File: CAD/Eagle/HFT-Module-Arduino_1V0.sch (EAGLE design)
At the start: 399 parts, among them Q0521 ABS07-32.768KHZ, Q0811 ABM03B-32.000MHZ, Q0911 ABM3B-16MHZ-10-R50-1-U, T1201 MMBT2222, T1202 MMBT2222, T1203 MMBT2222, U0111 STM32L4Z_144PIN_SMPS, U0431 PAM2305AAB120, U0601 LM4120IM5-3.0, U0611 MAX5217, U0631 CFPT-141-20MHZ, U0641 OPA354, U0701 Si5338, U0801 SX1276, U0901 AX5243, U0911 PE4259, U0921 PE4259, U0991 PE4259, U1101 MCP3911A0-E-SS, U1111 MAX5136AGTG+, U1121 OPA354, U1131 OPA354, U1141 OPA354, U1201 NHD-C0220BIZ_2X20CHARS, U1301 MPU-9250, U1311 MS5607-02BA03, U1321 SHT31-DIS, U1401 SOLARPANEL_3V3_5MA1_25MM_X_20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, U1402 SPV1040T, U1501 TS5A23166, U1601 SC189ZSKTRT, U1701 TS5A23166, U1801 TS5A23166, U1901 TS5A23166, X1261 TTE_EN11-HSM, X2001 MOLEX 105017-0001, X2101 SMA_SMT_AMPHENOL-901-143, SAM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, X2111 SMA_SMT_AMPHENOL-901-143, SAM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, X2201 CUI SJ1-3535NS, X2211 CUI SJ1-3535NS, X2311 2X20/90_1MM27_HARWIN_M50-3202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, X2312 2X20/90_1MM27_HARWIN_M50-3202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, X2321 2X20/90_1MM27_HARWIN_M50-3202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, X2322 2X20/90_1MM27_HARWIN_M50-3202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, X2331 2X20/90_1MM27_HARWIN_M50-3202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, X2332 2X20/90_1MM27_HARWIN_M50-3202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

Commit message: HW_1V0 - Initial setup of PCB
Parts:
- removed C0313, C0421, C0422, C0432, C0441, C0601, C0611, C0612, C0631, C0641, C0701, C0702, C0703, C0705, C1001, C1002, C1003, C1101, C1102, C1103, C1111, C1112, C1231, C1301, C1303, C1311, C1321, C1402, C1403, C1501, C1605, C1701, C1703, C1801, C1803, C1901, C1902, C1903, C1908, C1909: 100nF, rcl:C-EUC0603
- removed C0401, C0402, C0403, C0404, C0405, C0406, C0407, C0408, C0409, C0802, C0803, C0804, C0805, C0806, C0807: 100n, rcl:C-EUC0603
- removed C0410, C0423: 4.7uF, rcl:C-EUC0805
- removed C0412, C0715, C0716, C1302: 10nF, rcl:C-EUC0603
- removed C0413, C0442, C0622, C1211, C1221: 1uF, rcl:C-EUC0805
- removed C0431, C0444, C1401, C1404: 10uF, rcl:C-EUC0805
- removed C0451, C1601, C1607: 1F_EEC-S5R5H105N, df4iah_rcl:CPOL-EUW14MM_D8MM_P13MM5
- removed C0511, C0861: 1.5pF, rcl:C-EUC0603
- removed C0531: TZY2Z100AC01R00, df4iah_c-trimm:C-TRIMM3MM2_2MM5
- removed C0632: 100pF, rcl:C-EUC0603
- removed C0704: 220nF, rcl:C-EUC0603
- removed C0801: 1u, rcl:C-EUC0603
- removed C0811: 4.7p, df4iah_c-trimm:C-TRIMM3MM2_2MM5
- removed C0812: 4.7p, rcl:C-EUC0603
- removed C0841, C0850, C0858, C0872, C_AX_C1, C_AX_C2, C_AX_M2: 0pF, rcl:C-EUC0603
- removed C0843: 3.3pF, rcl:C-EUC0603
- removed C0844, C0846, C0851, C0852, C0873, C0875, C1113: 47pF, rcl:C-EUC0603
- removed C0853, C0863, C0871, C_AX_A2, C_AX_A3, C_AX_B2, C_AX_F2, C_AX_M1: 4.7pF, rcl:C-EUC0603
- removed C0854: 15nH, rcl:C-EUC0603
- removed C0856, C0859: 6.8pF, rcl:C-EUC0603
- removed C0857: 2.7pF, rcl:C-EUC0603
- removed C0862: 33pF, rcl:C-EUC0603
- removed C0864: 1.2pF, rcl:C-EUC0603
- removed C0865: 1.8pF, rcl:C-EUC0603
- removed C0911, C0921, C0999, C1261, C1262, C1271: 1nF, rcl:C-EUC0603
- removed C0991: 100pF HiQ, rcl:C-EUC0603
- removed C0992, C0993: 330pF HiQ, rcl:C-EUC0603
- removed C0994, C0996: 0nF HiQ, rcl:C-EUC0603
- removed C1104, C1105, C1131, C1141: 220nF, df4iah_rcl:C-EUC0603
- removed C1128, C1129: 100nF, df4iah_rcl:C-EUC0603
- removed C1132, C1142: 100uF, df4iah_rcl:C-EUC0805
- removed C1405: 0nF, rcl:C-EUC0603
- removed C1406, C1602, C1606: 47uF, rcl:C-EUC0805
- removed C2003: 1nF, df4iah_rcl:C-EUC0603
- removed C_AX_T1, C_AX_T2: 4.3pF, rcl:C-EUC0603
- removed D0451: CMAD6001, df4iah_diode:D_SOD923
- removed D1403, D1501: CRS08, df4iah_diode:CRS08
- removed H2401, H2402, H2403, H2404: MOUNT-PAD-ROUND2.8, holes:MOUNT-PAD-ROUND2.8
- removed L0411, L1102, L1112: 10uH, rcl:L-EUL2012C
- removed L0433: 2.2uH 14mR, df4iah_rcl:L-EU6.0X6.0MM
- removed L0842, L0862: 10nH, rcl:R-US_R0603
- removed L0851: 68nH, rcl:R-US_R0603
- removed L0856, L0858, L0995: 0R, rcl:R-US_R0603
- removed L0857: 12nH, rcl:R-US_R0603
- removed L0861: 33nH, rcl:R-US_R0603
- removed L0864: 6.2nH, rcl:R-US_R0603
- removed L0871: 18nH, rcl:R-US_R0603
- removed L1403: 33uH, df4iah_rcl:L-EU13.5X12.5MM
- removed L1604: 1.0uH 33mR, rcl:L-EUL5650M
- removed L_AX_1, L_AX_B1, L_AX_B2, L_AX_F1: 22nH, rcl:R-US_R0603
- removed L_AX_C1, L_AX_C2: 100nH, rcl:R-US_R0603
- removed L_AX_T1, L_AX_T2: 43nH, rcl:R-US_R0603
- removed PF2011: 1.1A/2.2A, rcl:R-EU_M1206
- removed Q0521: ABS07-32.768KHZ, df4iah_crystal:ABS07-32.768KHZ
- removed Q0811: ABM03B-32.000MHZ, df4iah_crystal:ABM03B-32.000MHZ
- removed Q0911: ABM3B-16MHZ-10-R50-1-U, df4iah_crystal:ABM03B-16.000MHZ
- removed R0201, R0202, R0211, R0212, R0221, R0222, R0231, R0232, R0441, R0612, R0613, R0811, R0845, R0874, R1404, R1405, R1406, R1409: 0R, rcl:R-EU_R0603
- removed R0241, R0242, R0243, R0251, R0252, R0253, R0254, R0261, R0262, R0263, R0269, R0271, R0272, R0273, R0274, R0275, R0276, R0277, R0281, R0282, R0283, R0284, R0285, R0286, R0287, R0288, R0289, R0290, R0291, R0292, R0293, R0294, R0295, R0296, R0642, R0713, R0714, R0723, R0724, R0731, R0732, R0735, R0736, R0743, R0744, R0802, R0803, R0831, R1021, R1041, R1051, R1061, R1106, R1107, R1108, R1109, R1114, R2310, R2311, R2312, R2313, R2314, R2315, R2316, R2317, R2318, R2320, R2321, R2322, R2323, R2324, R2325, R2326, R2327, R2328, R2330, R2331, R2332, R2333, R2334, R2335, R2336, R2337, R2338: 47R, rcl:R-EU_R0603
- removed R0311: 3.3kR, rcl:R-EU_R0603
- removed R0321, R0631, R1131, R1141, R1261, R1262, R1271: 10kR, rcl:R-EU_R0603
- removed R0611: open, rcl:R-EU_R0603
- removed R0621, R1031, R1032, R1407, R1412: 100kR, rcl:R-EU_R0603
- removed R0638, R0639: 50R, rcl:R-EU_R0603
- removed R0711, R0712: none, rcl:R-EU_R0603
- removed R0751, R0801, R0821: 100R, rcl:R-EU_R0603
- removed R0804, R0805, R0806, R0807: NC, rcl:R-EU_R0603
- removed R1104, R1105: 22kR, rcl:R-EU_R0603
- removed R1110, R1132, R1135, R1142, R1145, R1241, R1502, R1702, R1802, R1902: 33kR, rcl:R-EU_R0603
- removed R1201, R1205, R1208: 1.8kR, rcl:R-EU_R0603
- removed R1202: 5.2kR, rcl:R-EU_R0603
- removed R1203: 68R, rcl:R-EU_R0805
- removed R1204, R1207: 2.2kR, rcl:R-EU_R0603
- removed R1206, R1209: 10R, rcl:R-EU_R0805
- removed R1301: 68R, rcl:R-EU_R0603
- removed R1331, R1332: 3.9kR, rcl:R-EU_R0603
- removed R1408: 310kR, rcl:R-EU_R0603
- removed R1411: 1kR, rcl:R-EU_R0603
- removed R2002: 330kR, rcl:R-EU_R0603
- removed S0312: KSR223G, df4iah_switch:KSR223G_SMD_1POL
- removed SJ0121, SJ0401, SJ0421, SJ0422, SJ0423, SJ0424: (no value), df4iah_jumper:SJ
- removed T1201, T1202, T1203: MMBT2222, transistor:BC846
- removed TP_+1V2, TP_+1V2_MCU, TP_+3V3, TP_+3V3_20MHZ, TP_+3V3_HICUR, TP_+5V0, TP_+5V0_SOL, TP_+5V0_USB_SW, TP_VBAT, TP_VSOL: PTR1B1,27, testpad:PTR1B1,27
- removed TP_AX_ADC1, TP_AX_ADC2, TP_AX_IRQ, TP_AX_TCXO_EN, TP_SX_DIO0, TP_SX_DIO1, TP_SX_DIO2, TP_SX_DIO3, TP_SX_DIO4, TP_SX_DIO5, TP_SX_RXTX: PTR1TP06R, testpad:PTR1TP06R
- removed U0111: STM32L4Z_144PIN_SMPS, df4iah_stm32l4:STM32L4Z_144PIN_SMPS
- removed U0431: PAM2305AAB120, df4iah_powersupply:PAM2305
- removed U0601: LM4120IM5-3.0, df4iah_powersupply:LM4120IM5-3.0
- removed U0611: MAX5217, df4iah_dac:MAX5217
- removed U0631: CFPT-141-20MHZ, df4iah_osc:CFPT-141-20MHZ
- removed U0641, U1121, U1131, U1141: OPA354, df4iah_opamp:OPA354
- removed U0701: Si5338, df4iah_osc:SI5338
- removed U0801: SX1276, df4iah_rf:SX1276
- removed U0901: AX5243, df4iah_rf:AX5243
- removed U0911, U0921, U0991: PE4259, df4iah_rf:PE4259
- removed U1101: MCP3911A0-E-SS, df4iah_adc:MCP3911
- removed U1111: MAX5136AGTG+, df4iah_dac:MAX5136
- removed U1201: NHD-C0220BIZ_2X20CHARS, df4iah_lcd:NHD-C0220BIZ_2X20CHARS
- removed U1301: MPU-9250, df4iah_sensors:MPU-9250
- removed U1311: MS5607-02BA03, df4iah_sensors:MS5607-02BA03
- removed U1321: SHT31-DIS, df4iah_sensors:SHT31-DIS
- removed U1401: SOLARPANEL_3V3_5MA1_25MM_X_20MM, df4iah_supply:SOLARPANEL_3V3_5MA1_25MM_X_20MM
- removed U1402: SPV1040T, df4iah_powersupply:SPV1040
- removed U1501, U1701, U1801, U1901: TS5A23166, df4iah_sc-switches:TS5A23166
- removed U1601: SC189ZSKTRT, df4iah_powersupply:PAM2305
- removed X0301: (no value), df4iah_connector:HEADER-2X3
- removed X0322: (no value), df4iah_connector:HEADER-1X2
- removed X1261: TTE_EN11-HSM, df4iah_switch:TTE_EN11-HSM
- removed X2001: MOLEX 105017-0001, df4iah_connector:USB_MICRO-B_MOLEX
- removed X2101, X2111: SMA_SMT_AMPHENOL-901-143, SAMTEC SMA-J-P-H-RA-TH1, df4iah_connector:SMA_SMT_AMPHENOL-901-143
- removed X2201, X2211: CUI SJ1-3535NS, df4iah_connector:SJ1-353XNS_3MM5-STEREO-AUDIO-JACKS
- removed X2311, X2312, X2321, X2322, X2331, X2332: 2X20/90_1MM27_HARWIN_M50-3202045, df4iah_connector:2X20/90_1MM27_HARWIN_M50-3202045
- added H411, H412: MOUNT-PAD-ROUND2.8, holes:MOUNT-PAD-ROUND2.8
- added R111, R112, R113, R114, R115, R121, R122, R123, R124: 47R, rcl:R-EU_R0603
- added X111, X121: 2X20/90_1MM27_HARWIN_M50-3202045, df4iah_connector:2X20/90_1MM27_HARWIN_M50-3202045
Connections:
- removed net +1V2: C0444.1, C1901.1, L0433.1, TP_+1V2.TP, U0431.VOUT_FB, U1901.1, U1901.5
- removed net +1V5_UNUSED: SJ0424.2
- removed net +1V8_UNUSED: SJ0423.2
- removed net +2V5_UNUSED: SJ0422.2
- removed net +3V0_20MHZ_VCTCXO: C0611.1, C0631.1, U0601.VOUT, U0611.REF, U0631.VCC_3V0
- removed net +3V3_20MHZ: C0612.1, C0641.1, C1803.1, R0611.1, R0613.1, TP_+3V3_20MHZ.TP, U0611.VDD, U0641.V+, U1801.2, U1801.6
- removed net +3V3_HICUR: C0701.1, C0702.1, C0703.1, C0704.1, C0705.2, C1101.1, C1111.1, C1128.1, C1129.1, C1703.1, L1102.2, L1112.2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
- removed net +5V1_SOL: C1406.1, R1405.2, R1406.2, R1408.2, R1409.1, TP_+5V0_SOL.TP
- removed net 20MHZ_DAC_OUT: R0621.1, U0611.OUT
- removed net 20MHZ_XO: R0638.1, U0631.OUT
- removed net 20MHZ_XON: C0716.1, R0639.2, R0751.1
- removed net 20MHZ_XOP: C0715.1, R0638.2, R0751.2
- removed net AD_VCTCXO1: R0642.1, U0641.-IN, U0641.OUT
- removed net AUDIO_IN_L: C1104.1, X2201.TIP
- removed net AUDIO_IN_R: C1105.1, X2201.RING
- removed net AUDIO_OUT_L: C1132.2, X2211.TIP
- removed net AUDIO_OUT_L_OP: C1132.1, U1131.-IN, U1131.OUT
- removed net AUDIO_OUT_R: C1142.2, X2211.RING
- removed net AUDIO_OUT_R_OP: C1142.1, U1141.-IN, U1141.OUT
- removed net AX_16MHZ: R0714.1, R1021.2
- removed net AX_ADC1: R1031.1, TP_AX_ADC1.TP, U0901.GPADC1
- removed net AX_ADC2: R1032.1, TP_AX_ADC2.TP, U0901.GPADC2
- removed net AX_ANTN: C_AX_C2.1, C_AX_T2.1, L_AX_C2.1, U0901.ANTN
- removed net AX_ANTP: C_AX_C1.1, C_AX_T1.1, L_AX_C1.1, U0901.ANTP
- removed net AX_B1: C_AX_M1.1, L_AX_B1.1, L_AX_T1.2
- removed net AX_B2: C_AX_B2.1, C_AX_M2.1, L_AX_B2.2, L_AX_T2.2
- removed net AX_CLK16N: Q0911.1, U0901.CLK16N
- removed net AX_CLK16P: Q0911.2, U0901.CLK16P
- removed net AX_COMB: C_AX_A2.1, C_AX_B2.2, C_AX_F2.1, L_AX_B1.2, L_AX_F1.1
- removed net AX_GPIO1: R1061.2, TP_AX_TCXO_EN.TP, U0901.TCXO_EN
- removed net AX_IRQ: R1051.2, TP_AX_IRQ.TP, U0901.IRQ
- removed net AX_L1: L_AX_1.1, U0901.L1
- removed net AX_L2: L_AX_1.2, U0901.L2
- removed net AX_SYSCLK: R1021.1, U0901.SYSCLK
- removed net AX_T1: C_AX_T1.2, L_AX_T1.1
- removed net AX_T2: C_AX_T2.2, L_AX_T2.1
- removed net AX_VDD1: C1002.2, U0901.VDD_ANA@1
- removed net AX_VDD5: C1003.2, U0901.VDD_ANA@5
- removed net CH1_ANT: C0996.1, L0995.2, X2101.1
- removed net CH2_ANT: C_AX_A3.1, C_AX_F2.2, L_AX_F1.2, X2111.1
- removed net CLK0_N: R0743.2, X2332.4
- removed net CLK0_P: R0744.2, X2332.3
- removed net CLK1_N: R0735.2, X2322.4
- removed net CLK1_P: R0736.2, X2322.3
- removed net CLK2_N: R0731.2, X2312.4
- removed net CLK2_P: R0732.2, X2312.3
- removed net EVT_N: R2314.2, X2311.29
- removed net EVT_S: R2334.2, X2331.29
- removed net EVT_W: R2324.2, X2321.29
- removed net I2S_FS_IN_N: R2317.2, X2312.26
- removed net I2S_FS_IN_S: R2337.2, X2332.26
- removed net I2S_FS_IN_W: R2327.2, X2322.26
- removed net I2S_FS_OUT: R0284.2, X2312.20, X2322.20, X2332.20
- removed net I2S_MCLK_OUT: R0283.2, X2312.19, X2322.19, X2332.19
- removed net I2S_SCK_IN_N: R2315.2, X2312.23
- removed net I2S_SCK_IN_S: R2335.2, X2332.23
- removed net I2S_SCK_IN_W: R2325.2, X2322.23
- removed net I2S_SCK_OUT: R0281.2, X2312.17, X2322.17, X2332.17
- removed net I2S_SD_IN_N: R2316.2, X2312.24
- removed net I2S_SD_IN_S: R2336.2, X2332.24
- removed net I2S_SD_IN_W: R2326.2, X2322.24
- removed net I2S_SD_OUT: R0282.2, X2312.18, X2322.18, X2332.18
- removed net LCD_C1+: C1211.2, U1201.C1+
- removed net LCD_C1-: C1211.1, U1201.C1-
- removed net LCD_VOUT: C1221.1, U1201.VOUT
- removed net LED_B_B: R1207.1, R1208.2, T1203.B
- removed net LED_B_E: R1209.2, T1203.E
- removed net LED_B_K: T1203.C, U1201.KB
- removed net LED_G_B: R1204.1, R1205.2, T1202.B
- removed net LED_G_E: R1206.2, T1202.E
- removed net LED_G_K: T1202.C, U1201.KG
- removed net LED_R_B: R1201.1, R1202.2, T1201.B
- removed net LED_R_E: R1203.2, T1201.E
- removed net LED_R_K: T1201.C, U1201.KR
- removed net MAX5136_!READY: R1114.2, U1111.!READY
- removed net MAX5136_AVDD: C1112.2, L1112.1, U1111.AVDD, U1111.M/!Z
- removed net MAX5136_OUT0: R1131.1, U1111.OUT0
- removed net MAX5136_OUT0_R: C1131.1, R1131.2
- removed net MAX5136_OUT0_SUM: C1131.2, R1132.2, R1135.2, U1131.+IN
- removed net MAX5136_OUT1: R1141.1, U1111.OUT1
- removed net MAX5136_OUT1_R: C1141.1, R1141.2
- removed net MAX5136_OUT1_SUM: C1141.2, R1142.2, R1145.2, U1141.+IN
- removed net MAX5136_REF: C1113.1, U1111.REFI, U1111.REFO, U1121.+IN
- removed net MAX5136_REF_OP: R1132.1, R1142.1, U1121.-IN, U1121.OUT
- removed net MAX5217_!AUX: R0613.2, U0611.!AUX
- removed net MAX5217_ADDR: R0611.2, R0612.2, U0611.ADDR
- removed net MCP3911_!DR: R1106.1, U1101.!DR
- removed net MCP3911_CH0+: C1104.2, R1104.2, U1101.CH0+
- removed net MCP3911_CH1+: C1105.2, R1105.2, U1101.CH1+
- removed net MCP3911_MDAT0: R1108.1, U1101.MDAT0
- removed net MCP3911_MDAT1: R1109.1, U1101.MDAT1
- removed net MCP3911_REFINOUT: C1103.2, U1101.REFINOUT
- removed net MCP3911_SDO: R1107.1, U1101.SDO
- removed net MCU_AX_MISO: R1041.2, U0901.MISO
- removed net MCU_I2C1_SCL: R0201.2, X2312.7
- removed net MCU_I2C1_SDA: R0202.2, X2312.8
- removed net MCU_I2C2_SCL: R0211.2, X2322.7
- removed net MCU_I2C2_SDA: R0212.2, X2322.8
- removed net MCU_I2C3_SCL: R0221.2, X2332.7
- removed net MCU_I2C3_SDA: R0222.2, X2332.8
- removed net MCU_I2C4_SCL: R0231.2, R1332.1, U0611.SCL, U0701.SCL, U1201.SCL, U1301.SCL/SCLK, U1311.SCL_SCLK, U1321.SCL
- removed net MCU_I2C4_SDA: R0232.2, R1331.1, U0611.SDA, U0701.SDA, U1201.SDA, U1301.SDA/SDI, U1311.SDI_SDA, U1321.SDA
- removed net MCU_MCO: R0271.2, R0713.1
- removed net MCU_NRST: C0313.1, R0311.2, S0312.S, U0111.NRST
- removed net MCU_OUT_20MHZ_EN: R0273.2, R1802.2, U0601.EN, U1801.3, U1801.7
- removed net MCU_OUT_AUDIO_ADC_NRESET: R0261.2, R1110.2, U1101.!RESET
- removed net MCU_OUT_AUDIO_ADC_SEL: R0262.2, U1101.!CS
- removed net MCU_OUT_AUDIO_DAC_SEL: R0263.2, U1111.!CS
- removed net MCU_OUT_AX_SEL: R0253.2, U0901.SEL
- removed net MCU_OUT_HICUR_EN: R0275.2, R1702.2, U1701.3, U1701.7
- removed net MCU_OUT_LCD_NRST: R0272.2, R1241.2, U1201.RST
- removed net MCU_OUT_SX_SEL: R0254.2, U0801.NSS
- removed net MCU_OUT_VDD12_EN: R0276.2, R1902.2, U1901.3, U1901.7
- removed net MCU_OUT_VUSB_EN: R0274.2, R1502.2, U1501.3, U1501.7
- removed net MCU_SPI1_MISO: R0243.2, X2312.12, X2322.12, X2332.12
- removed net MCU_SPI1_MOSI: R0242.2, X2312.11, X2322.11, X2332.11
- removed net MCU_SPI1_SCK: R0241.2, X2312.13, X2322.13, X2332.13
- removed net MCU_SPI3_MOSI: R0252.2, U0801.MOSI, U0901.MOSI, U1101.SDI, U1111.DIN
- removed net MCU_SPI3_SCK: R0251.2, U0801.SCLK, U0901.CLK, U1101.SCK, U1111.SCLK
- removed net MCU_SX_TX_RX_CTRL: R0277.2, U0991.CTRL
- removed net MCU_VBAT: C0451.+, D0451.C, TP_VBAT.TP, U0111.VBAT
- removed net MCU_VDD: C0401.1, C0402.1, C0403.1, C0404.1, C0405.1, C0406.1, C0407.1, C0408.1, C0409.1, C0410.1, L0411.2, SJ0401.2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
- removed net MCU_VDD12: C1903.1, C1908.2, C1909.1, TP_+1V2_MCU.TP, U0111.VDD12_1, U0111.VDD12_2, U1901.2, U1901.6
- removed net MCU_VDDA: C0412.1, C0413.1, L0411.1, U0111.VDDA
- removed net MCU_VDDIO2: C0421.2, C0422.1, C0423.1, SJ0421.1, SJ0422.1, SJ0423.1, SJ0424.1, U0111.VDDIO2_1, U0111.VDDIO2_2
- removed net MCU_VREF_M: R0441.2, U0111.VREF-
- removed net MCU_VREF_P: C0441.2, C0442.2, U0111.VREF+
- removed net MCU_VSSA: SJ0121.2, U0111.VSSA
- removed net MCU_WAKEUP: R0269.2, X2311.33, X2321.33, X2331.33
- removed net MPU_INT: R1301.1, U1301.INT
- removed net MPU_REGOUT: C1303.1, U1301.REGOUT
- removed net MVP3911_AVDD: C1102.2, L1102.1, U1101.AVDD
- removed net PA0: R0292.1, U0111.PA0_WU
- removed net PA1: U0111.PA1
- removed net PA10: U0111.PA10, X2001.J_ID
- removed net PA13: U0111.PA13, X0301.1
- removed net PA14: U0111.PA14, X0301.5
- removed net PA15: U0111.PA15
- removed net PA2: R0289.1, U0111.PA2_WU
- removed net PA3: R1411.2, U0111.PA3
- removed net PA4: U0111.PA4
- removed net PA5: U0111.PA5
- removed net PA6: R0296.1, U0111.PA6
- removed net PA7: R1204.2, U0111.PA7
- removed net PA8: R0271.1, U0111.PA8
- removed net PA9: PF2011.1, U0111.PA9, X2001.J_VUSB
- removed net PA_USB_N: U0111.PA11, X2001.J_D-
- removed net PA_USB_P: U0111.PA12, X2001.J_D+
- removed net PB0: R1207.2, U0111.PB0
- removed net PB1: R0295.1, U0111.PB1
- removed net PB10: R1261.2, U0111.PB10
- removed net PB12: R1262.2, U0111.PB12
- removed net PB13: R2315.1, R2325.1, R2335.1, U0111.PB13
- removed net PB14: R1271.2, U0111.PB14
- removed net PB15: U0111.PB15
- removed net PB2: U0111.PB2
- removed net PB3: R2310.1, U0111.PB3
- removed net PB4: U0111.PB4
- removed net PB5: R2311.1, U0111.PB5
- removed net PB6: R2312.1, U0111.PB6
- removed net PB7: R2313.1, U0111.PB7
- removed net PB8: U0111.PB8
- removed net PB9: U0111.PB9
- removed net PC0: R0276.1, U0111.PC0
- removed net PC1: R0275.1, U0111.PC1
- removed net PC10: R0251.1, U0111.PC10
- removed net PC11: R0831.1, R1041.1, R1107.2, U0111.PC11
- removed net PC12: R0252.1, U0111.PC12
- removed net PC13: R0269.1, U0111.PC13_WU
- removed net PC14_MCU_OSC32_IN: C0531.E, Q0521.2, U0111.PC14_OSC32_IN
- removed net PC15_MCU_OSC32_OUT: C0511.1, Q0521.1, U0111.PC15_OSC32_OUT
- removed net PC2: R0274.1, U0111.PC2
- removed net PC3: R0273.1, U0111.PC3
- removed net PC4: R0293.1, U0111.PC4
- removed net PC5: R0294.1, U0111.PC5_WU
- removed net PC6: R1201.2, U0111.PC6
- removed net PC7: U0111.PC7
- removed net PC8: R1114.1, U0111.PC8
- removed net PC9: R0263.1, U0111.PC9
- removed net PD0: R1109.2, U0111.PD0
- removed net PD1: R1108.2, U0111.PD1
- removed net PD10: R2331.1, U0111.PD10
- removed net PD11: R2316.1, R2326.1, R2336.1, U0111.PD11
- removed net PD12: R2317.1, R2327.1, R2337.1, U0111.PD12
- removed net PD13: R0232.1, U0111.PD13
- removed net PD14: R2332.1, U0111.PD14
- removed net PD15: R2333.1, U0111.PD15
- removed net PD2: R1106.2, U0111.PD2
- removed net PD3: R0261.1, U0111.PD3
- removed net PD4: R0291.1, U0111.PD4
- removed net PD5: R0262.1, U0111.PD5
- removed net PD6: R0290.1, U0111.PD6
- removed net PD7: U0111.PD7, U0701.INTR
- removed net PD8: R0821.1, U0111.PD8
- removed net PD9: R2330.1, U0111.PD9
- removed net PE0: R2314.1, U0111.PE0
- removed net PE1: U0111.PE1
- removed net PE10: R0283.1, U0111.PE10
- removed net PE11: R0253.1, U0111.PE11
- removed net PE12: R0254.1, U0111.PE12
- removed net PE13: R0241.1, U0111.PE13
- removed net PE14: R0243.1, U0111.PE14
- removed net PE15: R0242.1, U0111.PE15
- removed net PE2: R2323.1, U0111.PE2
- removed net PE3: R0282.1, U0111.PE3
- removed net PE4: R2322.1, U0111.PE4
- removed net PE5: R2321.1, U0111.PE5
- removed net PE6: U0111.PE6_WU
- removed net PE7: R1051.1, U0111.PE7
- removed net PE8: R0281.1, U0111.PE8
- removed net PE9: R0284.1, U0111.PE9
- removed net PF0: R0212.1, U0111.PF0
- removed net PF1: R0211.1, U0111.PF1
- removed net PF10: R2324.1, U0111.PF10
- removed net PF11: U0111.PF11
- removed net PF12: R0272.1, U0111.PF12
- removed net PF13: R1301.2, U0111.PF13
- removed net PF14: R0231.1, U0111.PF14
- removed net PF15: U0111.PF15
- removed net PF2: R2320.1, U0111.PF2
- removed net PF3: R0642.2, U0111.PF3
- removed net PF4: U0111.PF4
- removed net PF5: U0111.PF5
- removed net PF6: R2318.1, U0111.PF6
- removed net PF7: R2328.1, U0111.PF7
- removed net PF8: R2338.1, U0111.PF8
- removed net PF9: R1412.1, U0111.PF9
- removed net PG0: R0277.1, U0111.PG0
- removed net PG1: R1061.1, U0111.PG1
- removed net PG10: R0286.1, U0111.PG10
- removed net PG11: R0288.1, U0111.PG11
- removed net PG12: R0287.1, U0111.PG12
- removed net PG13: R0202.1, U0111.PG13
- removed net PG14: R0201.1, U0111.PG14
- removed net PG2: R0802.2, U0111.PG2
- removed net PG3: R0803.2, U0111.PG3
- removed net PG4: R2334.1, U0111.PG4
- removed net PG5: U0111.PG5
- removed net PG6: U0111.PG6
- removed net PG7: R0221.1, U0111.PG7
- removed net PG8: R0222.1, U0111.PG8
- removed net PG9: R0285.1, U0111.PG9
- removed net PH0: R0724.1, U0111.PH0_OSC_IN
- removed net PH1: U0111.PH1_OSC_OUT
- removed net PH3_BOOT0: R0321.2, U0111.PH3_BOOT0, X0322.1
- removed net PN00: R2310.2, X2311.7
- removed net PN01: R2311.2, X2311.9
- removed net PN02: R2312.2, X2311.11
- removed net PN03: R2313.2, X2311.13
- removed net PS00: R2330.2, X2331.7
- removed net PS01: R2331.2, X2331.9
- removed net PS02: R2332.2, X2331.11
- removed net PS03: R2333.2, X2331.13
- removed net PW00: R2320.2, X2321.7
- removed net PW01: R2321.2, X2321.9
- removed net PW02: R2322.2, X2321.11
- removed net PW03: R2323.2, X2321.13
- removed net ROTENC_A: C1261.1, R1261.1, X1261.A
- removed net ROTENC_B: C1262.1, R1262.1, X1261.B
- removed net ROTENC_E: C1271.1, R1271.1, X1261.E
- removed net SI5338_CLK0A: R0744.1, U0701.CLK0A
- removed net SI5338_CLK0B: R0743.1, U0701.CLK0B
- removed net SI5338_CLK1A: R0736.1, U0701.CLK1A
- removed net SI5338_CLK1B: R0735.1, U0701.CLK1B
- removed net SI5338_CLK2A: R0732.1, U0701.CLK2A
- removed net SI5338_CLK2B: R0731.1, U0701.CLK2B
- removed net SI5338_CLK3A: R0724.2, U0701.CLK3A
- removed net SI5338_CLK3B: R0723.2, U0701.CLK3B
- removed net SI5338_CLK3B_2: R0723.1, U1101.OSC1
- removed net SI5338_IN1: R0711.2, U0701.IN1
- removed net SI5338_IN2: R0712.2, U0701.IN2
- removed net SI5338_IN3: R0713.2, U0701.IN3
- removed net SI5338_IN4: R0714.2, U0701.IN4
- removed net SI5338_IN5: C0715.2, U0701.IN5
- removed net SI5338_IN6: C0716.2, U0701.IN6
- removed net SI5338_IN_CLK1: R0711.1
- removed net SI5338_IN_CLK2: R0712.1
- removed net SPV_ICTRL_M: C1405.2, R1405.1, U1402.ICTRL_M
- removed net SPV_ICTRL_P: C1405.1, R1404.1, U1402.ICTRL_P
- removed net SPV_LX: D1403.A, L1403.1, R1412.2, U1402.LX
- removed net SPV_VCTRL: R1407.2, R1408.1, U1402.VCTRL
- removed net SPV_VOUT: C1403.1, C1404.1, D1403.C, R1404.2, R1406.1, U1402.VOUT
- removed net SW: L1604.2, U1601.SW
- removed net SX_ANT_1: C0993.1, U0991.RFC
- removed net SX_ANT_2: C0993.2, C0994.1, L0995.1
- removed net SX_DIO0: R0802.1, TP_SX_DIO0.TP, U0801.DIO0
- removed net SX_DIO1: R0803.1, TP_SX_DIO1.TP, U0801.DIO1
- removed net SX_DIO2: R0804.1, TP_SX_DIO2.TP, U0801.DIO2
- removed net SX_DIO2_2: R0804.2
- removed net SX_DIO3: R0805.1, TP_SX_DIO3.TP, U0801.DIO3
- removed net SX_DIO3_2: R0805.2
- removed net SX_DIO4: R0806.1, TP_SX_DIO4.TP, U0801.DIO4
- removed net SX_DIO4_2: R0806.2
- removed net SX_DIO5: R0807.1, TP_SX_DIO5.TP, U0801.DIO5
- removed net SX_DIO5_2: R0807.2
- removed net SX_HF_1: C0991.1, U0911.RFC
- removed net SX_HF_2: C0991.2, U0991.RF1
- removed net SX_LF_1: C0992.1, U0921.RFC
- removed net SX_LF_2: C0992.2, U0991.RF2
- removed net SX_MISO: R0831.2, U0801.MISO
- removed net SX_NRESET: R0821.2, U0801.!RESET
- removed net SX_RFI_HF: C0841.1, L0842.1, U0801.RFI_HF
- removed net SX_RFI_HF_2: C0843.1, C0844.1, L0842.2
- removed net SX_RFI_HF_3: C0844.2, R0845.1
- removed net SX_RFI_HF_4: C0846.1, R0845.2
- removed net SX_RFI_HF_5: C0846.2, U0911.RF2
- removed net SX_RFI_LF: C0871.1, L0871.1, U0801.RFI_LF
- removed net SX_RFI_LF_2: C0871.2, C0872.2, C0873.1
- removed net SX_RFI_LF_3: C0873.2, R0874.1
- removed net SX_RFI_LF_4: C0875.1, R0874.2
- removed net SX_RFI_LF_5: C0875.2, U0921.RF2
- removed net SX_RFO_HF: C0861.1, C0862.1, L0861.1, U0801.RFO_HF
- removed net SX_RFO_HF_2: C0862.2, L0862.1
- removed net SX_RFO_HF_3: C0863.1, C0864.1, L0862.2, L0864.1
- removed net SX_RFO_HF_4: C0864.2, C0865.1, L0864.2, U0911.RF1
- removed net SX_RFO_LF: C0853.1, C0854.1, L0851.1, U0801.RFO_LF
- removed net SX_RFO_LF_2: C0854.2, L0856.1
- removed net SX_RFO_LF_3: C0856.1, C0857.1, L0856.2, L0857.1
- removed net SX_RFO_LF_4: C0857.2, C0858.1, C0859.1, L0857.2, L0858.1
- removed net SX_RFO_LF_5: C0850.1, C0858.2, L0858.2, U0921.RF1
- removed net SX_RXTX: R0801.1, TP_SX_RXTX.TP, U0801.RXTX/RFMOD
- removed net SX_RXTX_2: R0801.2, U0911.CTRL, U0921.CTRL
- removed net SX_VR_ANA: C0806.2, U0801.VR_ANA
- removed net SX_VR_DIG: C0807.2, U0801.VR_DIG
- removed net SX_VR_PA: C0805.2, C0851.1, C0852.1, L0851.2, L0861.2, U0801.VR_PA
- removed net SX_XTA: C0811.E, Q0811.1, U0801.XTA
- removed net SX_XTB: R0811.1, U0801.XTB
- removed net SX_XTB_R: C0812.2, Q0811.2, R0811.2
- removed net TIMCAP_N: R2318.2, X2311.31
- removed net TIMCAP_S: R2338.2, X2331.31
- removed net TIMCAP_W: R2328.2, X2321.31
- removed net UART1_CTS_IN: R0288.2, X2311.26
- removed net UART1_RTS_OUT: R0287.2, X2311.25
- removed net UART1_RX_IN: R0286.2, X2311.24
- removed net UART1_TX_OUT: R0285.2, X2311.23
- removed net UART2_CTS_IN: R0292.2, X2321.26
- removed net UART2_RTS_OUT: R0291.2, X2321.25
- removed net UART2_RX_IN: R0290.2, X2321.24
- removed net UART2_TX_OUT: R0289.2, X2321.23
- removed net UART3_CTS_IN: R0296.2, X2331.26
- removed net UART3_RTS_OUT: R0295.2, X2331.25
- removed net UART3_RX_IN: R0294.2, X2331.24
- removed net UART3_TX_OUT: R0293.2, X2331.23
- removed net USB_SHIELD: C2003.2, R2002.2, X2001.SHIELD
- removed net VDD12_SW: L0433.2, U0431.SW
- removed net VDDUSB: C1501.1, PF2011.2, U1501.1, U1501.5, U1501.8
- removed net VSOL: C1401.1, C1402.1, L1403.2, R1411.1, TP_VSOL.TP, U1401.+VSOL, U1402.MPP_SET, U1402.XSHUT
- removed net VUSB_SW: D1501.A, TP_+5V0_USB_SW.TP, U1501.2, U1501.6
- removed net XO_LP: C0622.1, R0621.2, R0631.1, U0641.+IN
- removed net XO_VC: C0632.1, R0631.2, U0631.VC
- new net EXP_CLK_IN_N: X111.38
- new net EXP_CLK_IN_P: X111.37
- new net EXP_EVENT_IN: X121.11
- new net EXP_I2C_SCL_IN: X111.33
- new net EXP_I2C_SDA_INOUT: X111.34
- new net EXP_I2S_MSR_FS_OUT: R112.1
- new net EXP_I2S_MSR_FS_OUT_R: R112.2, X111.16
- new net EXP_I2S_MSR_MCLK_OUT: R111.1
- new net EXP_I2S_MSR_MCLK_OUT_R: R111.2, X111.15
- new net EXP_I2S_MSR_SCK_OUT: R113.1
- new net EXP_I2S_MSR_SCK_OUT_R: R113.2, X111.17
- new net EXP_I2S_MSR_SD_OUT: R114.1
- new net EXP_I2S_MSR_SD_OUT_R: R114.2, X111.18
- new net EXP_I2S_SLV_FS_IN: X111.22
- new net EXP_I2S_SLV_MCLK_IN: X111.21
- new net EXP_I2S_SLV_SCK_IN: X111.23
- new net EXP_I2S_SLV_SD_IN: X111.24
- new net EXP_PX0_INOUT: X121.33
- new net EXP_PX1__INOUT: X121.31
- new net EXP_PX2_INOUT: X121.29
- new net EXP_PX3_INOUT: X121.27
- new net EXP_SPI_MISO_OUT: R115.1
- new net EXP_SPI_MISO_OUT_R: R115.2, X111.30
- new net EXP_SPI_MOSI_IN: X111.29
- new net EXP_SPI_SCK_IN: X111.27
- new net EXP_TMRCAPT_OUT: R122.1
- new net EXP_TMRCAPT_OUT_R: R122.2, X121.9
- new net EXP_UART_CTS_IN: X121.15
- new net EXP_UART_RTS_OUT: R123.1
- new net EXP_UART_RTS_OUT_R: R123.2, X121.16
- new net EXP_UART_RX_IN: X121.17
- new net EXP_UART_TX_OUT: R124.1
- new net EXP_UART_TX_OUT_R: R124.2, X121.18
- new net EXP_WAKEUP_OUT: R121.1
- new net EXP_WAKEUP_OUT_R: R121.2, X121.7
- net +3V3: now also X111.3, X111.4, X121.37, X121.38; no longer C0431.1, C0432.1, C0601.1, C0801.1, C0802.2, C0803.2, C0804.2, C0911.1, C0921.1, C0999.1, C1001.1, C1231.1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
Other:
- note added: "Arduino sockets"
- note added: "Jumper field"
- note added: "Left"
- note added: "Right"
- note removed: "(1.0A out, 1.5MHz fixed)"
- note removed: "(1.5A out, 1.5MHz fixed)"
- note removed: "(replaces PAM2305)"
- note removed: "10MHz"
- note removed: "13.5mm x 12.5mm"
- note removed: "16MHz"
- note removed: "1V25"
- note removed: "20MHz"
- note removed: "3..10pF"
- note removed: "5mm x 5mm"
- note removed: "6mm x 6mm"
- note removed: "9-axis sensor: MPU-9250"
- note removed: "ADC3_IN6_20MHZ_PULL"
- note removed: "AUDIO IN"
- note removed: "AUDIO OUT"
- note removed: "Audio connectors"
- note removed: "Audio stereo A/D-Converter SPI"
- note removed: "Audio stereo D/A-Converter SPI"
- note removed: "BOOT0"
- note removed: "Baro sensor: MS5607-02BA03"
- note removed: "Boot configuration"
- note removed: "Clock distributor I2C addr: 0xE0/0xE1"
- note removed: "D/A-Converter: I2C addr: 0x38/0x39"
- note removed: "DC/DC boost converter"
- note removed: "DC/DC buck converter"
- note removed: "Debugging header"
- note removed: "Electronic switch for MCU SMTP ext. 1.2V"
- note removed: "Electronic switch for TCXO unit"
- note removed: "Electronic switch for USB <--> 5V"
- note removed: "Electronic switch for clock distribution unit"
- note removed: "HF: high / LF: low"
- note removed: "High prec. LDO"
- note removed: "I2C address = 1000100"
- note removed: "I2C address = 1101000"
- note removed: "I2C address = 1110110"
- note removed: "I2C2_INT"
- note removed: "I2C4 Termination"
- note removed: "Imax disabled"
- note removed: "Imax:50mV"
- note removed: "Impedance 100 Ohms"
- note removed: "Impedance 90 Ohms"
- note removed: "LC-Display I2C addr: 0x7C/0x7D"
- note removed: "LCD: 2x20 chars NHD-C0220BIZ-FS(RGB)-FBW-3VM-ND"
- note removed: "LITTLEFUSE 1206L050YR"
- note removed: "Low frequency oscillator"
- note removed: "MCU"
- note removed: "MCU VBAT"
- note removed: "MCU VDDA"
- note removed: "MCU VDDIO2 selection"
- note removed: "MCU VREF"
- note removed: "MCU switchboard"
- note removed: "MCU_EXTI2_SX_DIO0_TXRXDONE"
- note removed: "MCU_EXTI3_SX_DIO1_RXTO"
- note removed: "MCU_EXTI7_INTR_SI5338"
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
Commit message: HW_1V0 - CAD/Eagle - Arduino compatible headers added
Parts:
- added C201, C205: 100nF, rcl:C-EUC0805
- added C202, C206: 1uF, rcl:C-EUC0805
- added CN10: (no value), df4iah_connector:HEADER-2X17
- added CN7: (no value), df4iah_connector:HEADER-2X10
- added CN8, X211: (no value), df4iah_connector:HEADER-2X8
- added CN9: (no value), df4iah_connector:HEADER-2X15
- added R1, R2, R3, R4, R5, R6, R7, R8, R9: 0R, rcl:R-EU_R0805
- added R231, R232: 3k3R, rcl:R-EU_R0805
- added X201: (no value), df4iah_connector:HEADER-2X2
- added X221: (no value), df4iah_connector:HEADER-2X5
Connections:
- removed net EXP_PX1__INOUT: X121.31
- new net A0: CN9.1
- new net A1: CN9.3
- new net A2: CN9.5
- new net A3: CN9.7
- new net A4_SDA: CN7.4, CN9.9, R4.2, R6.1
- new net A5_SCL: CN7.2, CN9.11, R3.2, R5.1
- new net AREF: CN7.6
- new net D0_RX: CN10.16, R1.1
- new net D10_SS: CN7.16, X221.1, X221.3, X221.5, X221.7, X221.9
- new net D11_MOSI: CN7.14, R9.1
- new net D12_MISO: CN7.12, R8.1
- new net D13_SCK: CN7.10, R7.1
- new net D1_TX: CN10.14, R2.1
- new net D2_INT0: CN10.12
- new net D3_INT1: CN10.10
- new net D4_T0: CN10.8
- new net D5_T1: CN10.6
- new net D6: CN10.4
- new net D7: CN10.2
- new net D8: CN7.20
- new net D9: CN7.18
- new net EXP_PX1_INOUT: X121.31, X211.12, X221.6
- new net IOREF: CN8.3, X201.1, X201.3
- new net NRST: CN8.5, X211.1, X211.11, X211.13, X211.15, X211.3, X211.5, X211.7, X211.9
- new net VIN: CN8.15
- net +3V3: now also C201.1, C202.1, CN8.7, R231.2, R232.2, X201.4
- net +5V0: now also C205.1, C206.1, CN8.9, X201.2
- net EXP_EVENT_IN: now also X211.6
- net EXP_I2C_SCL_IN: now also R232.1, R3.1, R5.2
- net EXP_I2C_SDA_INOUT: now also R231.1, R4.1, R6.2
- net EXP_PX0_INOUT: now also X211.14, X221.8
- net EXP_PX2_INOUT: now also X211.10, X221.4
- net EXP_PX3_INOUT: now also X211.8, X221.2
- net EXP_TMRCAPT_OUT: now also X211.4
- net EXP_UART_RX_IN: now also R2.2
- net EXP_UART_TX_OUT: now also R1.2
- net EXP_WAKEUP_OUT: now also X211.2
- net GND: now also C201.2, C202.2, C205.2, C206.2, CN7.8, CN8.11, CN8.13
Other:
- note added: "D.C."

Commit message: HW_1V0 - CAD/Eagle - components placed first round
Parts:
- removed R1, R8: 0R, rcl:R-EU_R0805
- removed R111, R112, R113, R114, R123: 47R, rcl:R-EU_R0603
- added X231: (no value), df4iah_connector:HEADER-2X2
- R115, R121, R122, R124: device rcl:R-EU_R0603 -> rcl:R-EU_R0805
- renumbered R2 to R331, R3 to R312, R4 to R311, R5 to R313, R6 to R314, R7 to R321, R9 to R323
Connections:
- removed net EXP_I2S_MSR_FS_OUT: R112.1
- removed net EXP_I2S_MSR_MCLK_OUT: R111.1
- removed net EXP_I2S_MSR_SCK_OUT: R113.1
- removed net EXP_I2S_MSR_SD_OUT: R114.1
- removed net EXP_SPI_MISO_OUT: R115.1
- removed net EXP_UART_RTS_OUT: R123.1
- removed net EXP_UART_TX_OUT: R1.2, R124.1
- new net N$1: R231.1, X231.2
- new net N$2: R232.1, X231.4
- net D0_RX: now also R124.1; no longer R1.1
- net D12_MISO: now also R115.1; no longer R8.1
- net EXP_I2C_SCL_IN: now also X231.3; no longer R232.1
- net EXP_I2C_SDA_INOUT: now also X231.1; no longer R231.1
- net EXP_I2S_MSR_FS_OUT_R: no longer R112.2
- net EXP_I2S_MSR_MCLK_OUT_R: no longer R111.2
- net EXP_I2S_MSR_SCK_OUT_R: no longer R113.2
- net EXP_I2S_MSR_SD_OUT_R: no longer R114.2
- net EXP_SPI_MOSI_IN: now also R323.2
- net EXP_SPI_SCK_IN: now also R321.2
- net EXP_UART_RTS_OUT_R: no longer R123.2
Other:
- note added: "I2C TERM"

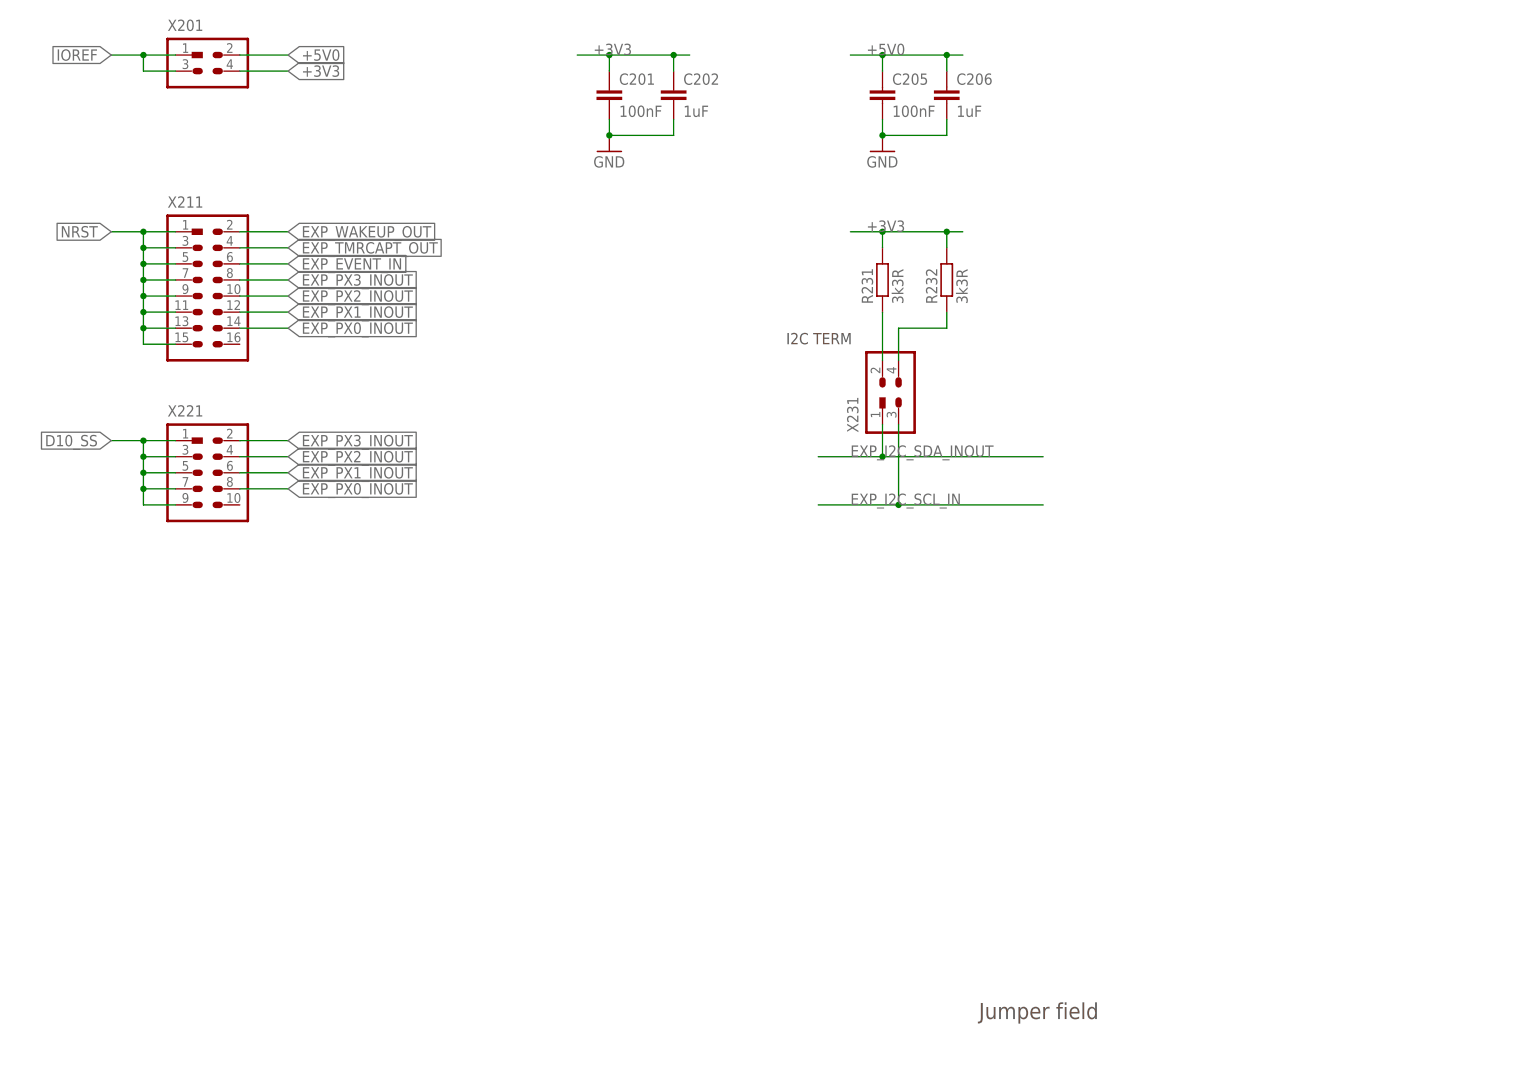
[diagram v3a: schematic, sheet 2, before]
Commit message: HW_1V0 - CAD/Eagle - placing finished, routing started
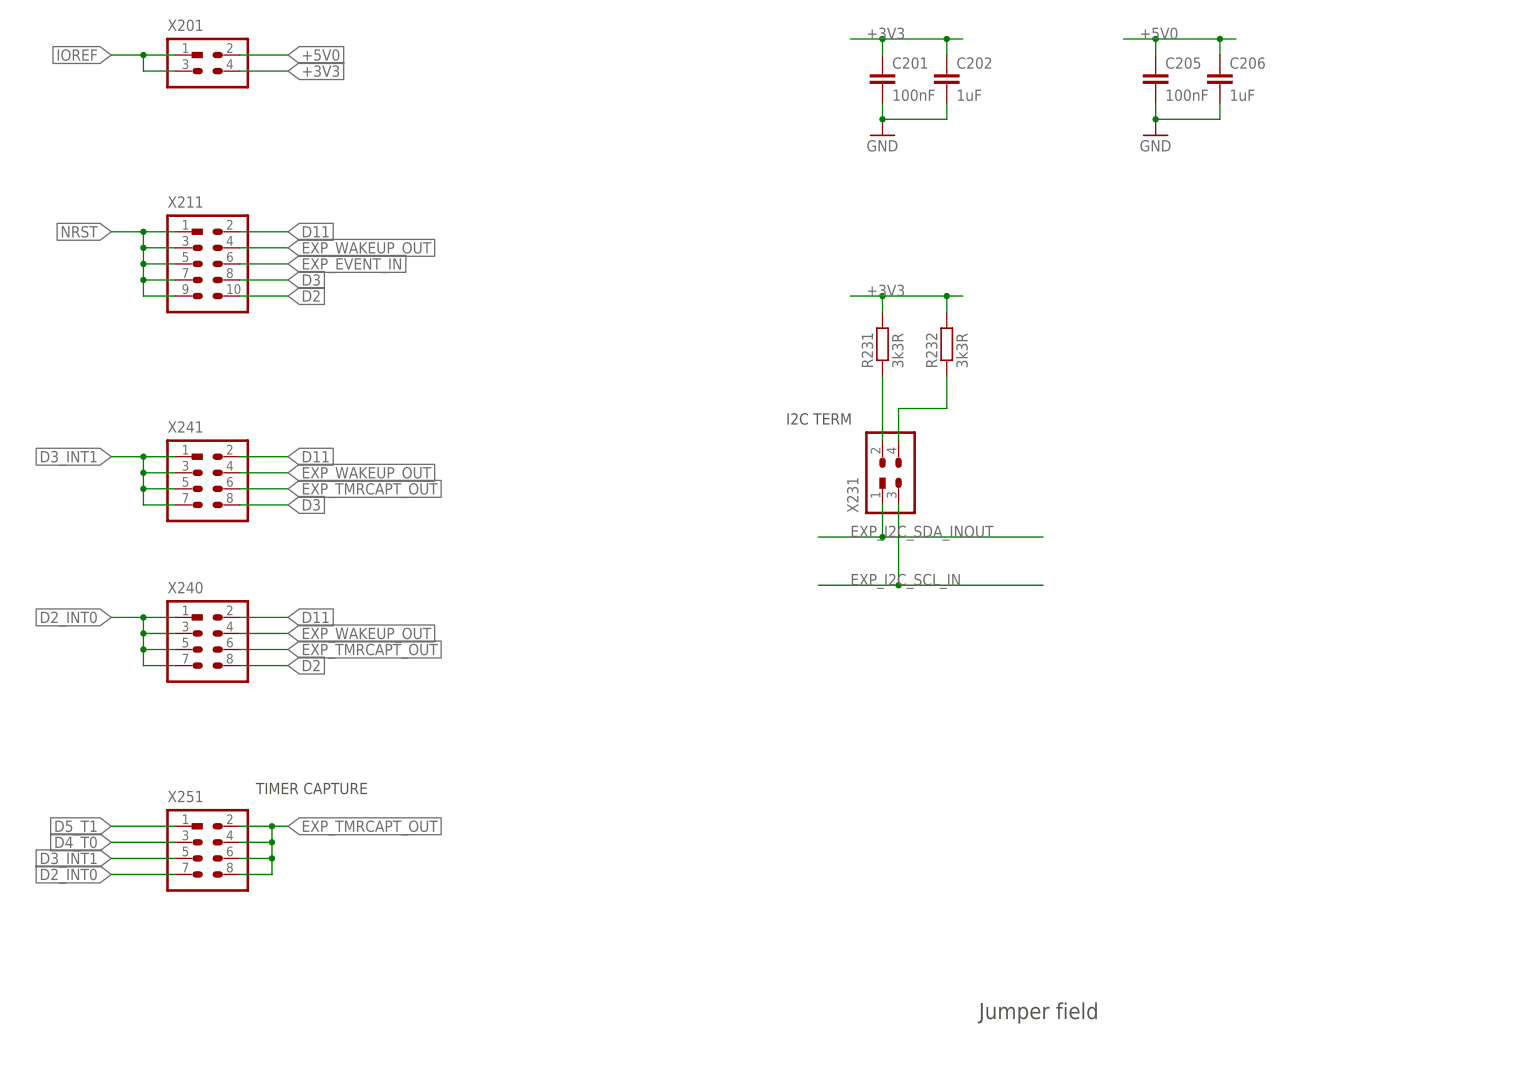
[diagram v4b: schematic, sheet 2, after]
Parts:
- removed X221: (no value), df4iah_connector:HEADER-2X5
- added R125, R126, R127, R128, R152, R153, R154, R155, R156, R157, R158, R159, R160, R161: 47R, rcl:R-EU_R0805
- added R324, R334, R335, R341, R342, R343, R344: 0R, rcl:R-EU_R0805
- added X240, X241, X251: (no value), df4iah_connector:HEADER-2X4
- X211: device df4iah_connector:HEADER-2X8 -> df4iah_connector:HEADER-2X5
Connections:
- net N$1 renamed SDA_TERM
- net N$2 renamed SCL_TERM
- new net D10: R160.1, R324.2
- new net D11: R161.1, X211.2, X240.2, X241.2
- new net D2: R152.1, X211.10, X240.8
- new net D3: R153.1, X211.8, X241.8
- new net D4: R154.1, R334.2
- new net D5: R155.1, R335.2
- new net EXP_PX0_INOUT_R: R128.2, X121.33
- new net EXP_PX1_INOUT_R: R127.2, X121.31
- new net EXP_PX2_INOUT_R: R126.2, X121.29
- new net EXP_PX3_INOUT_R: R125.2, X121.27
- net A0: now also R341.2
- net A1: now also R342.2
- net A2: now also R343.2
- net A3: now also R344.2
- net D10_SS: now also R324.1; no longer X221.1, X221.3, X221.5, X221.7, X221.9
- net D2_INT0: now also X240.1, X240.3, X240.5, X240.7, X251.7
- net D3_INT1: now also X241.1, X241.3, X241.5, X241.7, X251.5
- net D4_T0: now also R334.1, X251.3
- net D5_T1: now also R335.1, X251.1
- net D6: now also R156.1
- net D7: now also R157.1
- net D8: now also R158.1
- net D9: now also R159.1
- net EXP_I2S_MSR_FS_OUT_R: now also R160.2
- net EXP_I2S_MSR_MCLK_OUT_R: now also R161.2
- net EXP_I2S_MSR_SCK_OUT_R: now also R159.2
- net EXP_I2S_MSR_SD_OUT_R: now also R158.2
- net EXP_I2S_SLV_FS_IN: now also R156.2
- net EXP_I2S_SLV_MCLK_IN: now also R157.2
- net EXP_I2S_SLV_SCK_IN: now also R155.2
- net EXP_I2S_SLV_SD_IN: now also R154.2
- net EXP_PX0_INOUT: now also R128.1, R341.1; no longer X121.33, X211.14, X221.8
- net EXP_PX1_INOUT: now also R127.1, R342.1; no longer X121.31, X211.12, X221.6
- net EXP_PX2_INOUT: now also R126.1, R343.1; no longer X121.29, X211.10, X221.4
- net EXP_PX3_INOUT: now also R125.1, R344.1; no longer X121.27, X211.8, X221.2
- net EXP_TMRCAPT_OUT: now also X240.6, X241.6, X251.2, X251.4, X251.6, X251.8; no longer X211.4
- net EXP_UART_CTS_IN: now also R153.2
- net EXP_UART_RTS_OUT_R: now also R152.2
- net EXP_WAKEUP_OUT: now also X211.4, X240.4, X241.4; no longer X211.2
- net NRST: no longer X211.11, X211.13, X211.15
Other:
- note added: "TIMER CAPTURE"
- moved on the sheet: C201, C202, C205, C206, R231, R232, R331, X231
